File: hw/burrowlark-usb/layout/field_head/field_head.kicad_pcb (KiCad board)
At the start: 2 copper layers, 27 parts

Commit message: Remove Burrowlark infrasound hardware and refresh board previews
Keep DAQUSB-01 magnetometer-only across the circuit, routed PCB, BOM, review schematic and native routing snapshot. Publish the refreshed render in the main README and add population regression checks.

Validation: 125 pin checks, clean ERC/DRC, native routing replay, 3 Burrowlark regression tests and lab unit tests pass. Full lab builds pass; hardware regressions stop on unrelated DAQHAT-01 assembly registry/source mismatches.
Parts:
- removed C5: , elec:Capacitor_SMD__C_0603_1608Metric
- removed U3: , elec:Groundlark__DLVR_E1BS
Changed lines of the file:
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@@
-		)
-	)
-	(footprint "elec:Groundlark__DLVR_E1BS"
-		(layer "F.Cu")
-		(at 250 0 0)
-		(property "Reference" "U3"
-			(at 0 -5 0)
-			(layer "F.SilkS")
-			(effects
-				(font
-					(size 0.8 0.8)
-					(thickness 0.12)
-				)
-			)
-		)
-		(property "Value" ""
-			(at 0 5 0)
-			(layer "F.Fab")
-			(effects
-				(font
-					(size 0.8 0.8)
-					(thickness 0.12)
-				)
-			)
-		)
-		(property "Datasheet" ""
-			(at 0 0 0)
-			(layer "F.Fab")
-			(hide yes)
-			(effects
-				(font
-					(size 1.27 1.27)
-					(thickness 0.15)
-				)
-			)
-		)
-		(property "Description" ""
-			(at 0 0 0)
-			(layer "F.Fab")
-			(hide yes)
-			(effects
-				(font
-					(size 1.27 1.27)
-					(thickness 0.15)
-				)
-			)
-		)
-		(property "atopile_address" "u3"
-			(at 0 0 0)
-			(layer "User.9")
-			(hide yes)
-		)
-		(fp_circle
-			(center -3.43 -5.5)
-			(end -3.18 -5.5)
-			(stroke
-				(width 0.12)
-				(type solid)
-			)
-			(fill no)
-			(layer "F.SilkS")
-		)
-		(fp_rect
-			(start -3.03 -5.8)
-			(end 10.3 -0.5)
-			(stroke
-				(width 0.05)
-				(type solid)
-			)
-			(fill no)
-			(layer "F.CrtYd")
-		)
-		(fp_rect
-			(start -2.73 -5.5)
-			(end 10 -0.8)
-			(stroke
-				(width 0.1)
-				(type solid)
-			)
-			(fill no)
-			(layer "F.Fab")
-		)
-		(pad "1" thru_hole rect
-			(at 0 0)
-			(size 1.8 1.8)
-			(drill 1)
-			(layers "*.Cu" "*.Mask")
-			(remove_unused_layers no)
-			(net 5 "GND")
-		)
-		(pad "2" thru_hole oval
-			(at 2.54 0)
-			(size 1.8 1.8)
-			(drill 1)
-			(layers "*.Cu" "*.Mask")
-			(remove_unused_layers no)
-			(net 42 "V3_SENSOR")
-		)
-		(pad "3" thru_hole oval
-			(at 5.08 0)
-			(size 1.8 1.8)
-			(drill 1)
-			(layers "*.Cu" "*.Mask")
-			(remove_unused_layers no)
-			(net 12 "SDA")
-		)
-		(pad "4" thru_hole oval
-			(at 7.62 0)
-			(size 1.8 1.8)
-			(drill 1)
-			(layers "*.Cu" "*.Mask")
-			(remove_unused_layers no)
-			(net 13 "SCL")
-		)
-		(embedded_fonts no)
-	)
-	(footprint "elec:Capacitor_SMD__C_0603_1608Metric"
-		(layer "F.Cu")
-		(at 260 0 0)
-		(descr "Capacitor SMD 0603 (1608 Metric), square (rectangular) end terminal, IPC-7351 nominal, (Body size source: IPC-SM-782 page 76, https://www.pcb-3d.com/wordpress/wp-content/uploads/ipc-sm-782a_amendment_1_and_2.pdf), generated with kicad-footprint-generator")
-		(tags "capacitor")
-		(property "Reference" "C5"
-			(at 0 -1.43 0)
-			(layer "F.SilkS")
-			(effects
-				(font
-					(size 1 1)
-					(thickness 0.15)
-				)
-			)
-		)
-		(property "Value" ""
-			(at 0 1.43 0)
-			(layer "F.Fab")
-			(effects
-				(font
-					(size 1 1)
-					(thickness 0.15)
-				)
-			)
-		)
-		(property "atopile_address" "c5"
-			(at 0 0 0)
-			(layer "User.9")
-			(hide yes)
-		)
-		(attr smd)
-		(fp_line
-			(start -0.14058 -0.51)
-			(end 0.14058 -0.51)
-			(stroke
-				(width 0.12)
-				(type solid)
-			)
-			(layer "F.SilkS")
-		)
-		(fp_line
-			(start -0.14058 0.51)
-			(end 0.14058 0.51)
-			(stroke
-				(width 0.12)
-				(type solid)
-			)
-			(layer "F.SilkS")
-		)
-		(fp_rect
-			(start -1.48 -0.73)
-			(end 1.48 0.73)
-			(stroke
-				(width 0.05)
-				(type solid)
-			)
-			(fill no)
-			(layer "F.CrtYd")
-		)
-		(fp_rect
-			(start -0.8 -0.4)
-			(end 0.8 0.4)
-			(stroke
-				(width 0.1)
-				(type solid)
-			)
-			(fill no)
-			(layer "F.Fab")
-		)
-		(pad "1" smd roundrect
-			(at -0.775 0)
-			(size 0.9 0.95)
-			(layers "F.Cu" "F.Mask" "F.Paste")
-			(net 42 "V3_SENSOR")
-			(roundrect_rratio 0.25)
-		)
-		(pad "2" smd roundrect
-			(at 0.775 0)
-			(size 0.9 0.95)
-			(layers "F.Cu" "F.Mask" "F.Paste")
-			(net 5 "GND")
-			(roundrect_rratio 0.25)
-		)
-		(embedded_fonts no)
-		(model "${KICAD9_3DMODEL_DIR}/Capacitor_SMD.3dshapes/C_0603_1608Metric.step"
-			(offset
-				(xyz 0 0 0)
-			)
-			(scale
-				(xyz 1 1 1)
-			)
-			(rotate
-				(xyz 0 0 0)
-			)
 		)
 	)

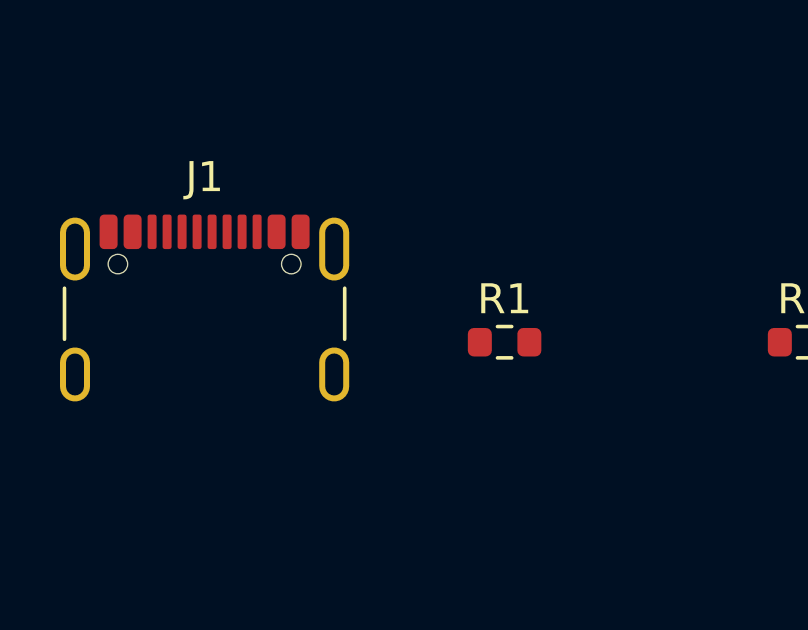
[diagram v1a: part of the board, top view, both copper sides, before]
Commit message: Add SHT45 enclosure climate sensing to Burrowlark
Add Sensirion SHT45-AD1B-R2 U6 and switched-rail bypass C10, with JLCPCB C5221601 stock evidence. Synchronize circuit, routed PCB, native SES, schematic, BOM, README render and browser model.

Publish CRC-checked raw climate sensor 17 through simulation, recording and replay. Add enclosure controls, independent fault/recovery checks and protocol fixtures. The isolated software profile passes 213 tests; Burrowlark DRC/ERC and copper replay pass. Full hardware regression remains blocked by pre-existing assembly registry mismatches. MCU firmware and physical qualification remain pending.
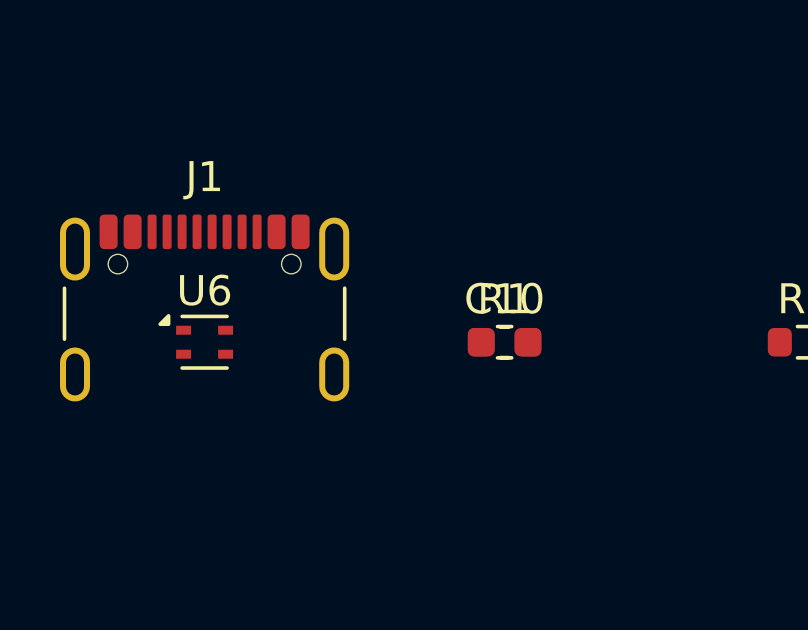
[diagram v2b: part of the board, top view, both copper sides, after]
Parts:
- added C10: , elec:Capacitor_SMD__C_0603_1608Metric, F.Cu at (10.0, 0.00)
- added U6: , elec:SHT45, F.Cu at (0.00, 0.00)
